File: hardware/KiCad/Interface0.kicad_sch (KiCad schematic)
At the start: 3 parts

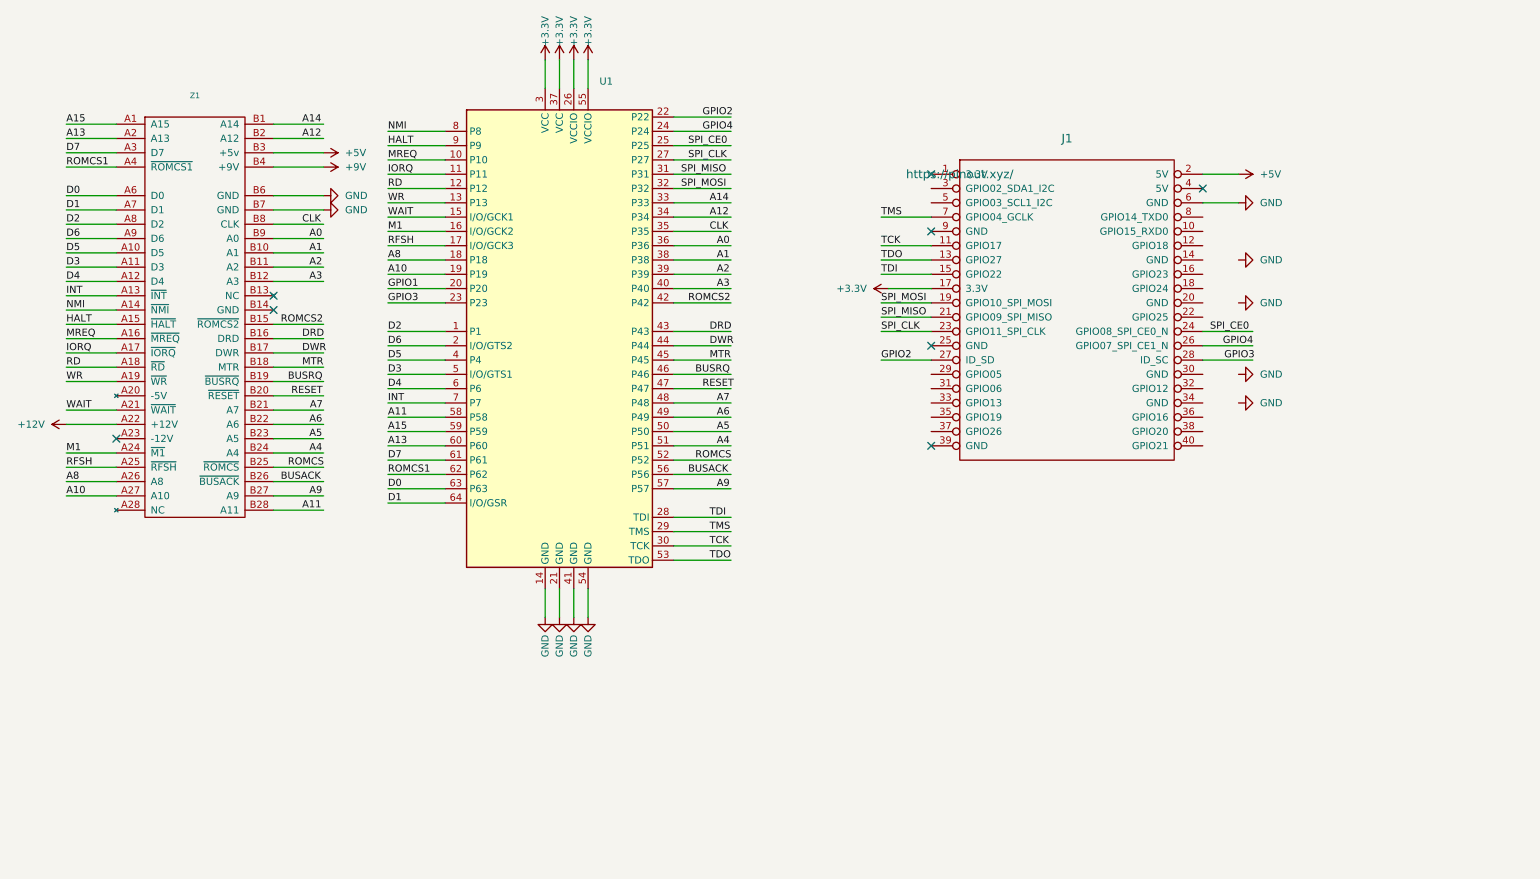
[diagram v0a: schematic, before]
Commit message: Incorporate Álvaro Lopes tips
- connect MREQ/IOREQ & SPI_CLK to GCKx
- connect RESET to GSR
- restucture the other pins to make it cleaner
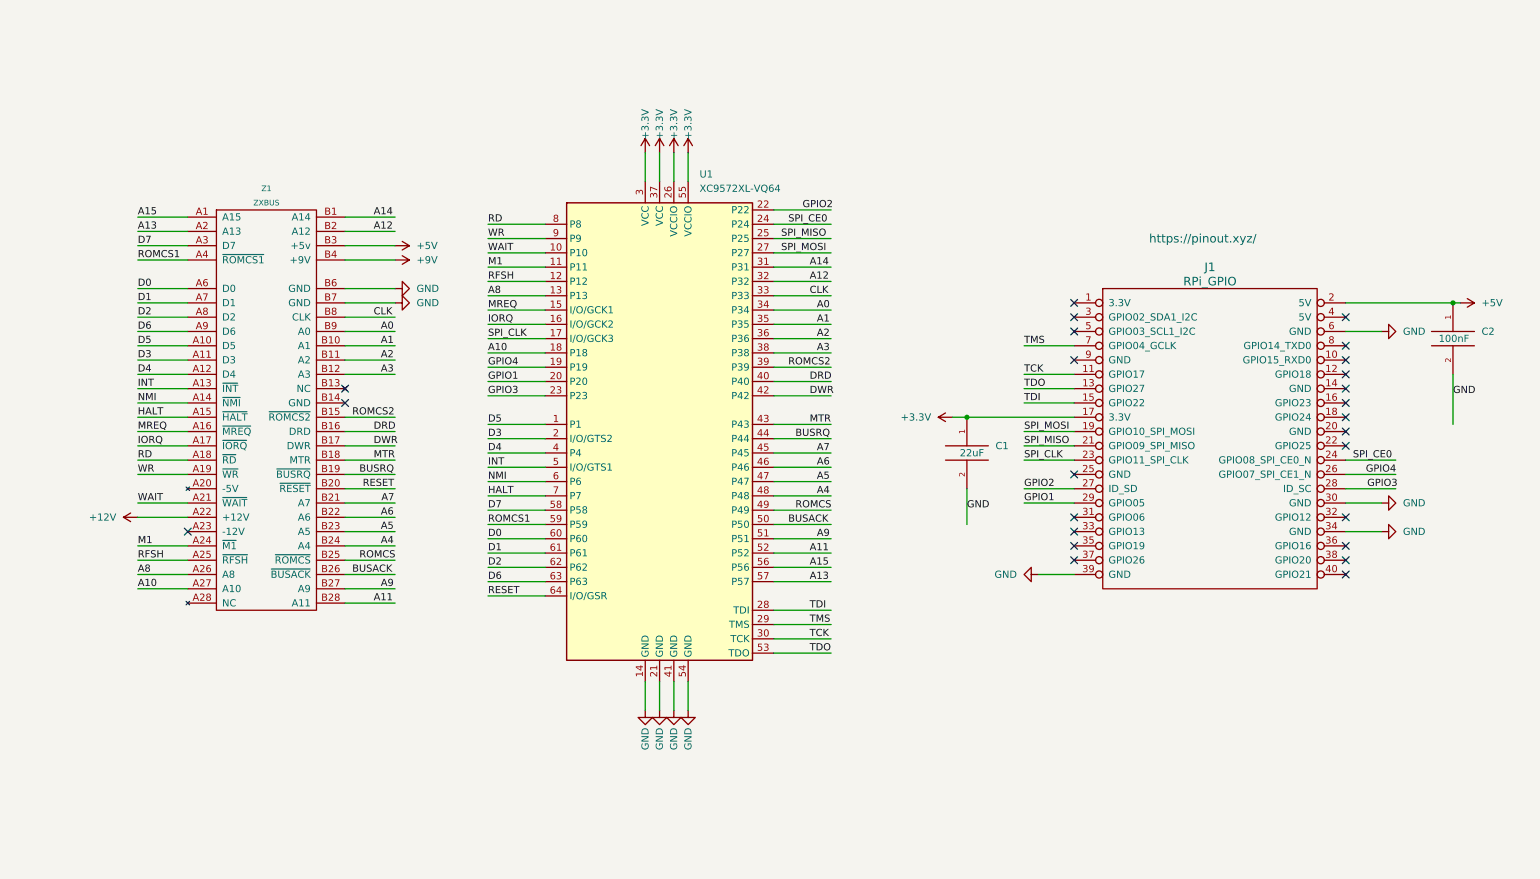
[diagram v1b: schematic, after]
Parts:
- added C1: 22uF, Capacitor_SMD:C_0603_1608Metric_Pad1.08x0.95mm_HandSolder, symbol pspice:CAP
- added C2: 100nF, Capacitor_THT:CP_Radial_Tantal_D5.0mm_P2.50mm, symbol pspice:CAP
- J1: value (none) -> RPi_GPIO; footprint (none) -> Connector_Samtec_HLE_THT:Samtec_HLE-120-02-xx-DV-TE_2x20_P2.54mm_Horizontal
- U1: value (none) -> XC9572XL-VQ64; footprint (none) -> Package_QFP:TQFP-64_10x10mm_P0.5mm
- Z1: value (none) -> ZXBUS; footprint (none) -> ZX:ZX_Bus_Edge_Connector
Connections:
- net +3V3: now also C1.1
- net +5V: now also C2.1
- net A0: now also U1.34 (P34); no longer U1.36 (P36)
- net A1: now also U1.35 (P35); no longer U1.38 (P38)
- net A10: now also U1.18 (P18); no longer U1.19 (P19)
- net A11: now also U1.52 (P52); no longer U1.58 (P58)
- net A12: now also U1.32 (P32); no longer U1.34 (P34)
- net A13: now also U1.57 (P57); no longer U1.60 (P60)
- net A14: now also U1.31 (P31); no longer U1.33 (P33)
- net A15: now also U1.56 (P56); no longer U1.59 (P59)
- net A2: now also U1.36 (P36); no longer U1.39 (P39)
- net A3: now also U1.38 (P38); no longer U1.40 (P40)
- net A4: now also U1.48 (P48); no longer U1.51 (P51)
- net A5: now also U1.47 (P47); no longer U1.50 (P50)
- net A6: now also U1.46 (P46); no longer U1.49 (P49)
- net A7: now also U1.45 (P45); no longer U1.48 (P48)
- net A8: now also U1.13 (P13); no longer U1.18 (P18)
- net A9: now also U1.51 (P51); no longer U1.57 (P57)
- net BUSACK: now also U1.50 (P50); no longer U1.56 (P56)
- net BUSRQ: now also U1.44 (P44); no longer U1.46 (P46)
- net CLK: now also U1.33 (P33); no longer U1.35 (P35)
- net D0: now also U1.60 (P60); no longer U1.63 (P63)
- net D1: now also U1.61 (P61); no longer U1.64 (I/O/GSR)
- net D2: now also U1.62 (P62); no longer U1.1 (P1)
- net D3: now also U1.2 (I/O/GTS2); no longer U1.5 (I/O/GTS1)
- net D4: now also U1.4 (P4); no longer U1.6 (P6)
- net D5: now also U1.1 (P1); no longer U1.4 (P4)
- net D6: now also U1.63 (P63); no longer U1.2 (I/O/GTS2)
- net D7: now also U1.58 (P58); no longer U1.61 (P61)
- net DRD: now also U1.40 (P40); no longer U1.43 (P43)
- net DWR: now also U1.42 (P42); no longer U1.44 (P44)
- net GND: now also J1.30 (GND), J1.34 (GND), J1.39 (GND), C1.2, C2.2
- net GPIO1: now also J1.29 (GPIO05)
- net GPIO4: now also U1.19 (P19); no longer U1.24 (P24)
- net HALT: now also U1.7 (P7); no longer U1.9 (P9)
- net INT: now also U1.5 (I/O/GTS1); no longer U1.7 (P7)
- net IORQ: now also U1.16 (I/O/GCK2); no longer U1.11 (P11)
- net M1: now also U1.11 (P11); no longer U1.16 (I/O/GCK2)
- net MREQ: now also U1.15 (I/O/GCK1); no longer U1.10 (P10)
- net MTR: now also U1.43 (P43); no longer U1.45 (P45)
- net NMI: now also U1.6 (P6); no longer U1.8 (P8)
- net RD: now also U1.8 (P8); no longer U1.12 (P12)
- net RESET: now also U1.64 (I/O/GSR); no longer U1.47 (P47)
- net RFSH: now also U1.12 (P12); no longer U1.17 (I/O/GCK3)
- net ROMCS: now also U1.49 (P49); no longer U1.52 (P52)
- net ROMCS1: now also U1.59 (P59); no longer U1.62 (P62)
- net ROMCS2: now also U1.39 (P39); no longer U1.42 (P42)
- net SPI_CE0: now also U1.24 (P24); no longer U1.25 (P25)
- net SPI_CLK: now also U1.17 (I/O/GCK3); no longer U1.27 (P27)
- net SPI_MISO: now also U1.25 (P25); no longer U1.31 (P31)
- net SPI_MOSI: now also U1.27 (P27); no longer U1.32 (P32)
- net WAIT: now also U1.10 (P10); no longer U1.15 (I/O/GCK1)
- net WR: now also U1.9 (P9); no longer U1.13 (P13)
- no-connect marks 8 -> 25
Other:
- company: (none) -> https://zx.licentia.eu
- title: (none) -> Interface 0
- moved on the sheet: J1, U1, Z1

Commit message: Prepare for first release
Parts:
- C1: footprint Capacitor_SMD:C_0603_1608Metric_Pad1.08x0.95mm_HandSolder -> Capacitor_THT:CP_Radial_Tantal_D7.0mm_P2.50mm
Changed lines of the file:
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@@
     (rev "3.1")
     (company "https://zx.licentia.eu")
+    (comment 1 "Raspberry PI 0 (2) base ZX Interface")
   )
   (junction (at 182.88 82.55) (diameter 0) (color 0 0 0 0)
@@
       (effects (font (size 1.27 1.27)) (justify left))
     )
-    (property "Footprint" "Capacitor_SMD:C_0603_1608Metric_Pad1.08x0.95mm_HandSolder" (id 2) (at 182.88 88.9 0)
+    (property "Footprint" "Capacitor_THT:CP_Radial_Tantal_D7.0mm_P2.50mm" (id 2) (at 182.88 88.9 0)
       (effects (font (size 1.27 1.27)) hide)
     )
@@
     )
     (path "/49d32279-5a88-4fad-a526-fb238ce9f4dc"
-      (reference "C1") (unit 1) (value "22uF") (footprint "Capacitor_SMD:C_0603_1608Metric_Pad1.08x0.95mm_HandSolder")
+      (reference "C1") (unit 1) (value "22uF") (footprint "Capacitor_THT:CP_Radial_Tantal_D7.0mm_P2.50mm")
     )
     (path "/bbb04a5e-7369-45f7-b462-9bd277c4027f"

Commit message: PI_CE0 acts as a clock and we must wire it to a clock pin
Wire the Z80 CPU clock to the remaing one.
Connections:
- net A12: now also U1.33 (P33); no longer U1.32 (P32)
- net A14: now also U1.32 (P32); no longer U1.31 (P31)
- net CLK: now also U1.15 (I/O/GCK1); no longer U1.33 (P33)
- net GPIO1: now also U1.22 (P22); no longer U1.20 (P20)
- net GPIO2: now also U1.24 (P24); no longer U1.22 (P22)
- net GPIO4: now also U1.31 (P31); no longer U1.19 (P19)
- net HALT: now also U1.20 (P20); no longer U1.7 (P7)
- net IORQ: now also U1.12 (P12); no longer U1.16 (I/O/GCK2)
- net MREQ: now also U1.7 (P7); no longer U1.15 (I/O/GCK1)
- net RFSH: now also U1.19 (P19); no longer U1.12 (P12)
- net SPI_CE0: now also U1.17 (I/O/GCK3); no longer U1.24 (P24)
- net SPI_CLK: now also U1.16 (I/O/GCK2); no longer U1.17 (I/O/GCK3)
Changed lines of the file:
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@@
     (effects (font (size 1.27 1.27)) (justify left bottom))
   )
-  (label "SPI_CE0" (at 151.13 48.26 0)
+  (label "SPI_CE0" (at 97.79 68.58 0)
     (effects (font (size 1.27 1.27)) (justify left bottom))
   )
@@
     (effects (font (size 1.27 1.27)) (justify left bottom))
   )
+  (label "HALT" (at 97.79 76.2 0)
+    (effects (font (size 1.27 1.27)) (justify left bottom))
+  )
   (label "GPIO4" (at 253.7507 92.71 0)
     (effects (font (size 1.27 1.27)) (justify left bottom))
@@
     (effects (font (size 1.27 1.27)) (justify left bottom))
   )
-  (label "A14" (at 154.94 55.88 0)
-    (effects (font (size 1.27 1.27)) (justify left bottom))
-  )
   (label "WR" (at 35.56 92.71 0)
     (effects (font (size 1.27 1.27)) (justify left bottom))
@@
     (effects (font (size 1.27 1.27)) (justify left bottom))
   )
-  (label "CLK" (at 154.94 60.96 0)
-    (effects (font (size 1.27 1.27)) (justify left bottom))
-  )
-  (label "GPIO4" (at 97.79 73.66 0)
-    (effects (font (size 1.27 1.27)) (justify left bottom))
-  )
-  (label "SPI_CLK" (at 97.79 68.58 0)
+  (label "GPIO4" (at 153.67 55.88 0)
+    (effects (font (size 1.27 1.27)) (justify left bottom))
+  )
+  (label "SPI_CLK" (at 97.79 66.04 0)
     (effects (font (size 1.27 1.27)) (justify left bottom))
   )
@@
     (effects (font (size 1.27 1.27)) (justify left bottom))
   )
+  (label "IORQ" (at 97.79 58.42 0)
+    (effects (font (size 1.27 1.27)) (justify left bottom))
+  )
   (label "A3" (at 156.21 71.12 0)
     (effects (font (size 1.27 1.27)) (justify left bottom))
@@
     (effects (font (size 1.27 1.27)) (justify left bottom))
   )
+  (label "A12" (at 154.94 60.96 0)
+    (effects (font (size 1.27 1.27)) (justify left bottom))
+  )
   (label "A8" (at 97.79 60.96 0)
     (effects (font (size 1.27 1.27)) (justify left bottom))
@@
     (effects (font (size 1.27 1.27)) (justify left bottom))
   )
+  (label "GPIO3" (at 97.79 78.74 0)
+    (effects (font (size 1.27 1.27)) (justify left bottom))
+  )
   (label "ROMCS2" (at 73.66 82.55 0)
     (effects (font (size 1.27 1.27)) (justify left bottom))
@@
     (effects (font (size 1.27 1.27)) (justify left bottom))
   )
-  (label "GPIO2" (at 153.67 45.72 0)
-    (effects (font (size 1.27 1.27)) (justify left bottom))
-  )
   (label "TCK" (at 193.04 74.93 0)
     (effects (font (size 1.27 1.27)) (justify left bottom))
@@
     (effects (font (size 1.27 1.27)) (justify left bottom))
   )
-  (label "MREQ" (at 97.79 63.5 0)
-    (effects (font (size 1.27 1.27)) (justify left bottom))
-  )
   (label "NMI" (at 97.79 93.98 0)
     (effects (font (size 1.27 1.27)) (justify left bottom))
@@
     (effects (font (size 1.27 1.27)) (justify left bottom))
   )
-  (label "GPIO3" (at 97.79 78.74 0)
+  (label "RFSH" (at 97.79 73.66 0)
     (effects (font (size 1.27 1.27)) (justify left bottom))
   )
@@
     (effects (font (size 1.27 1.27)) (justify left bottom))
   )
-  (label "HALT" (at 97.79 96.52 0)
+  (label "GPIO2" (at 153.67 48.26 0)
     (effects (font (size 1.27 1.27)) (justify left bottom))
   )
@@
     (effects (font (size 1.27 1.27)) (justify left bottom))
   )
-  (label "IORQ" (at 97.79 66.04 0)
-    (effects (font (size 1.27 1.27)) (justify left bottom))
-  )
-  (label "A12" (at 154.94 58.42 0)
+  (label "A14" (at 154.94 58.42 0)
     (effects (font (size 1.27 1.27)) (justify left bottom))
   )
@@
     (effects (font (size 1.27 1.27)) (justify left bottom))
   )
-  (label "GPIO1" (at 97.79 76.2 0)
-    (effects (font (size 1.27 1.27)) (justify left bottom))
-  )
   (label "BUSACK" (at 73.66 110.49 0)
     (effects (font (size 1.27 1.27)) (justify left bottom))
   )
+  (label "GPIO1" (at 153.67 45.72 0)
+    (effects (font (size 1.27 1.27)) (justify left bottom))
+  )
   (label "D2" (at 97.79 109.22 0)
     (effects (font (size 1.27 1.27)) (justify left bottom))
@@
     (effects (font (size 1.27 1.27)) (justify left bottom))
   )
-  (label "RFSH" (at 97.79 58.42 0)
+  (label "CLK" (at 97.79 63.5 0)
     (effects (font (size 1.27 1.27)) (justify left bottom))
   )
@@
     (effects (font (size 1.27 1.27)) (justify left bottom))
   )
+  (label "MREQ" (at 97.79 96.52 0)
+    (effects (font (size 1.27 1.27)) (justify left bottom))
+  )

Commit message: Use custom IO protocol
Use GPCLK1 as a master clock
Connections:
- net GPIO4 is gone; now on net GPIO3: J1.26 (GPIO07_SPI_CE1_N), U1.31 (P31)
- net GPIO1: now also J1.27 (ID_SD), U1.24 (P24); no longer J1.29 (GPIO05), U1.22 (P22)
- net GPIO2: now also J1.28 (ID_SC), U1.23 (P23); no longer J1.27 (ID_SD), U1.24 (P24)
- net GPIO3: no longer J1.28 (ID_SC), U1.23 (P23)
- net SPI_CE0 renamed IO
- net IO: now also U1.22 (P22); no longer U1.17 (I/O/GCK3)
- net SPI_CLK renamed IO_CLK
- net IO_CLK: now also U1.17 (I/O/GCK3); no longer U1.16 (I/O/GCK2)
- net SPI_MISO renamed MISO
- net SPI_MOSI renamed MOSI
- new net MASTER_CLK: J1.29 (GPIO05), U1.16 (I/O/GCK2)
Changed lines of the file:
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@@
     (stroke (width 0) (type default) (color 0 0 0 0))
   )
-  (wire (pts (xy 193.04 97.79) (xy 201.93 97.79))
+  (wire (pts (xy 190.5 97.79) (xy 201.93 97.79))
     (stroke (width 0) (type default) (color 0 0 0 0))
   )
@@
     (stroke (width 0) (type default) (color 0 0 0 0))
   )
-  (wire (pts (xy 97.79 66.04) (xy 107.95 66.04))
+  (wire (pts (xy 95.25 66.04) (xy 107.95 66.04))
     (stroke (width 0) (type default) (color 0 0 0 0))
   )
@@
     (effects (font (size 1.27 1.27)) (justify left bottom))
   )
-  (label "SPI_CE0" (at 97.79 68.58 0)
-    (effects (font (size 1.27 1.27)) (justify left bottom))
-  )
   (label "MTR" (at 154.94 83.82 0)
     (effects (font (size 1.27 1.27)) (justify left bottom))
@@
     (effects (font (size 1.27 1.27)) (justify left bottom))
   )
-  (label "GPIO3" (at 254 95.25 0)
+  (label "GPIO2" (at 254 95.25 0)
     (effects (font (size 1.27 1.27)) (justify left bottom))
   )
@@
     (effects (font (size 1.27 1.27)) (justify left bottom))
   )
-  (label "GPIO4" (at 253.7507 92.71 0)
+  (label "IO" (at 157.48 45.72 0)
+    (effects (font (size 1.27 1.27)) (justify left bottom))
+  )
+  (label "GPIO3" (at 253.7507 92.71 0)
     (effects (font (size 1.27 1.27)) (justify left bottom))
   )
@@
     (effects (font (size 1.27 1.27)) (justify left bottom))
   )
-  (label "SPI_MOSI" (at 193.04 85.09 0)
+  (label "MOSI" (at 193.04 85.09 0)
     (effects (font (size 1.27 1.27)) (justify left bottom))
   )
@@
     (effects (font (size 1.27 1.27)) (justify left bottom))
   )
-  (label "GPIO1" (at 193.04 97.79 0)
+  (label "MASTER_CLK" (at 190.5 97.79 0)
     (effects (font (size 1.27 1.27)) (justify left bottom))
   )
@@
     (effects (font (size 1.27 1.27)) (justify left bottom))
   )
-  (label "GPIO4" (at 153.67 55.88 0)
-    (effects (font (size 1.27 1.27)) (justify left bottom))
-  )
-  (label "SPI_CLK" (at 97.79 66.04 0)
+  (label "GPIO3" (at 153.67 55.88 0)
     (effects (font (size 1.27 1.27)) (justify left bottom))
   )
@@
     (effects (font (size 1.27 1.27)) (justify left bottom))
   )
+  (label "IO_CLK" (at 97.79 68.58 0)
+    (effects (font (size 1.27 1.27)) (justify left bottom))
+  )
   (label "A12" (at 77.47 49.53 0)
     (effects (font (size 1.27 1.27)) (justify left bottom))
   )
-  (label "GPIO2" (at 193.04 95.25 0)
+  (label "GPIO1" (at 193.04 95.25 0)
     (effects (font (size 1.27 1.27)) (justify left bottom))
   )
@@
     (effects (font (size 1.27 1.27)) (justify left bottom))
   )
-  (label "SPI_MISO" (at 193.04 87.63 0)
+  (label "MISO" (at 193.04 87.63 0)
     (effects (font (size 1.27 1.27)) (justify left bottom))
   )
@@
     (effects (font (size 1.27 1.27)) (justify left bottom))
   )
-  (label "GPIO3" (at 97.79 78.74 0)
+  (label "GPIO2" (at 97.79 78.74 0)
     (effects (font (size 1.27 1.27)) (justify left bottom))
   )
@@
     (effects (font (size 1.27 1.27)) (justify left bottom))
   )
-  (label "SPI_CLK" (at 193.04 90.17 0)
+  (label "IO_CLK" (at 193.04 90.17 0)
     (effects (font (size 1.27 1.27)) (justify left bottom))
   )
@@
     (effects (font (size 1.27 1.27)) (justify left bottom))
   )
-  (label "GPIO2" (at 153.67 48.26 0)
+  (label "GPIO1" (at 153.67 48.26 0)
     (effects (font (size 1.27 1.27)) (justify left bottom))
   )
@@
     (effects (font (size 1.27 1.27)) (justify left bottom))
   )
-  (label "GPIO1" (at 153.67 45.72 0)
-    (effects (font (size 1.27 1.27)) (justify left bottom))
-  )
   (label "D2" (at 97.79 109.22 0)
     (effects (font (size 1.27 1.27)) (justify left bottom))
   )
+  (label "MASTER_CLK" (at 95.25 66.04 0)
+    (effects (font (size 1.27 1.27)) (justify left bottom))
+  )
   (label "D7" (at 97.79 99.06 0)
     (effects (font (size 1.27 1.27)) (justify left bottom))
@@
     (effects (font (size 1.27 1.27)) (justify left bottom))
   )
-  (label "SPI_MISO" (at 149.86 50.8 0)
+  (label "MISO" (at 154.94 50.8 0)
     (effects (font (size 1.27 1.27)) (justify left bottom))
   )
@@
     (effects (font (size 1.27 1.27)) (justify left bottom))
   )
-  (label "SPI_CE0" (at 251.46 90.17 0)
+  (label "IO" (at 256.54 90.17 0)
     (effects (font (size 1.27 1.27)) (justify left bottom))
   )
@@
     (effects (font (size 1.27 1.27)) (justify left bottom))
   )
-  (label "SPI_MOSI" (at 149.86 53.34 0)
-    (effects (font (size 1.27 1.27)) (justify left bottom))
-  )
+  (label "MOSI" (at 154.94 53.34 0)
+    (effects (font (size 1.27 1.27)) (justify left bottom))
+  )

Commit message: Nuke HALT & RFSH and connect them to RPi
Add first verilog implementation
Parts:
- added D1: 1N4001, Diode_THT:D_DO-41_SOD81_P10.16mm_Horizontal, symbol Diode:1N4001
- added U2: TSR_1-2450, Converter_DCDC:Converter_DCDC_TRACO_TSR-1_THT, symbol Regulator_Switching:TSR_1-2450
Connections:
- net +5V: now also D1.1 (K)
- net +9V: now also U2.1 (Vin)
- net GND: now also U2.2 (GND)
- net GPIO1: now also J1.22 (GPIO25); no longer J1.27 (ID_SD)
- net GPIO2: now also J1.26 (GPIO07_SPI_CE1_N); no longer J1.28 (ID_SC)
- net GPIO3: now also J1.13 (GPIO27); no longer J1.26 (GPIO07_SPI_CE1_N)
- net HALT: no longer U1.20 (P20)
- net MASTER_CLK: now also J1.7 (GPIO04_GCLK); no longer J1.29 (GPIO05)
- net RFSH: no longer U1.19 (P19)
- net TCK: now also J1.16 (GPIO23); no longer J1.11 (GPIO17)
- net TDO: now also J1.11 (GPIO17); no longer J1.13 (GPIO27)
- net TMS: now also J1.18 (GPIO24); no longer J1.7 (GPIO04_GCLK)
- new net: D1.2 (A), U2.3 (Vout)
- new net GPIO4: J1.27 (ID_SD), U1.20 (P20)
- new net GPIO5: J1.28 (ID_SC), U1.19 (P19)
- no-connect marks 25 -> 22
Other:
- moved on the sheet: C1, C2, J1

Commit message: Swap p25 with p23 to free one FB from FB4
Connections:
- net GPIO2: now also U1.25 (P25); no longer U1.23 (P23)
- net MISO: now also U1.23 (P23); no longer U1.25 (P25)
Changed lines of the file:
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@@
     (effects (font (size 1.27 1.27)) (justify right bottom))
-  )
-  (label "GPIO2" (at 97.79 78.74 0)
-    (effects (font (size 1.27 1.27)) (justify left bottom))
   )
   (label "ROMCS1" (at 35.56 54.61 0)
@@
     (effects (font (size 1.27 1.27)) (justify left bottom))
   )
+  (label "GPIO2" (at 153.67 50.8 0)
+    (effects (font (size 1.27 1.27)) (justify left bottom))
+  )
   (label "HALT" (at 35.56 82.55 0)
     (effects (font (size 1.27 1.27)) (justify left bottom))
@@
     (effects (font (size 1.27 1.27)) (justify left bottom))
   )
-  (label "MISO" (at 154.94 50.8 0)
-    (effects (font (size 1.27 1.27)) (justify left bottom))
-  )
   (label "MREQ" (at 97.79 96.52 0)
     (effects (font (size 1.27 1.27)) (justify left bottom))
@@
     (effects (font (size 1.27 1.27)) (justify left bottom))
   )
+  (label "MISO" (at 97.79 78.74 0)
+    (effects (font (size 1.27 1.27)) (justify left bottom))
+  )
